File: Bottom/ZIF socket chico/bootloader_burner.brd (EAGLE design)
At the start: 65.4 x 64 mm, 6 parts, among them J1 ZIFSOCKET-28-3", Y1 16MHz

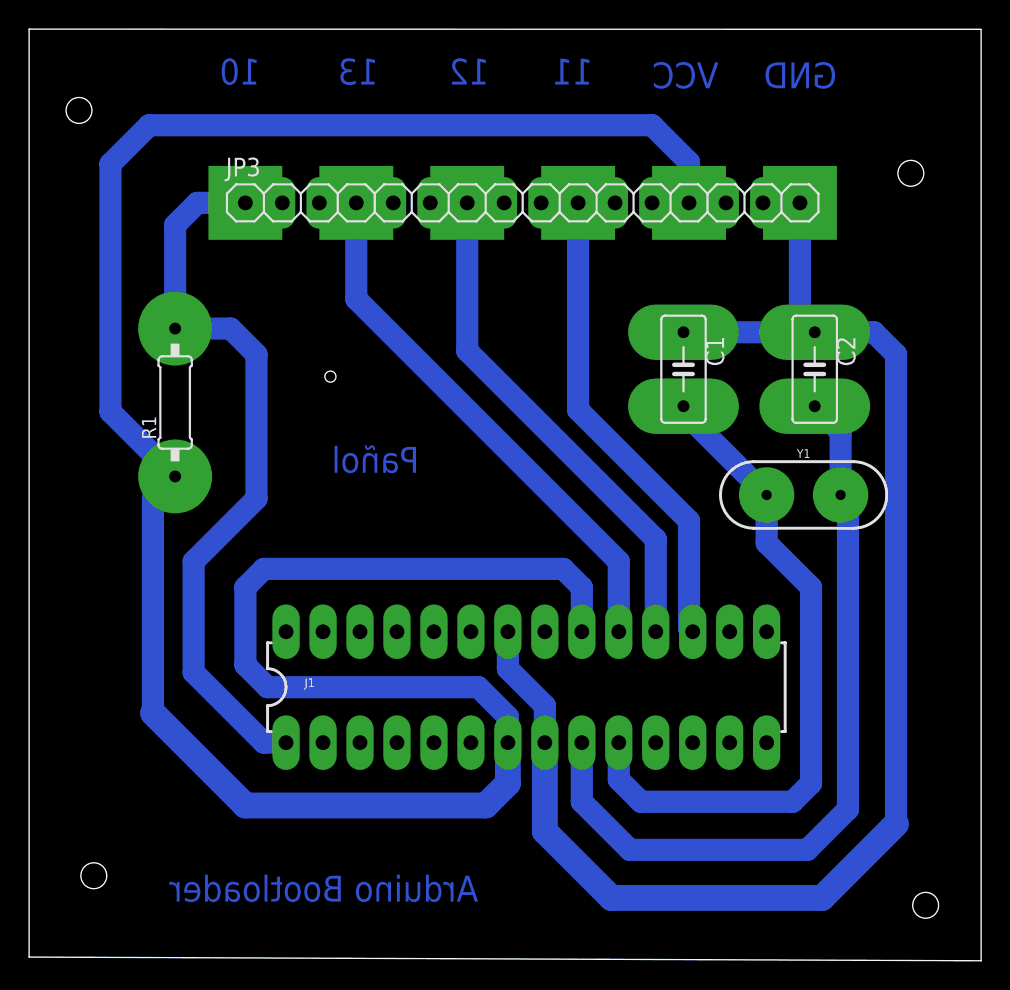
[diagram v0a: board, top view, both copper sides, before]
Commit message: Cambie la plaqueta para el zif socket chico para que queden ordenados los pines para conectar la plaqueta al Arduino
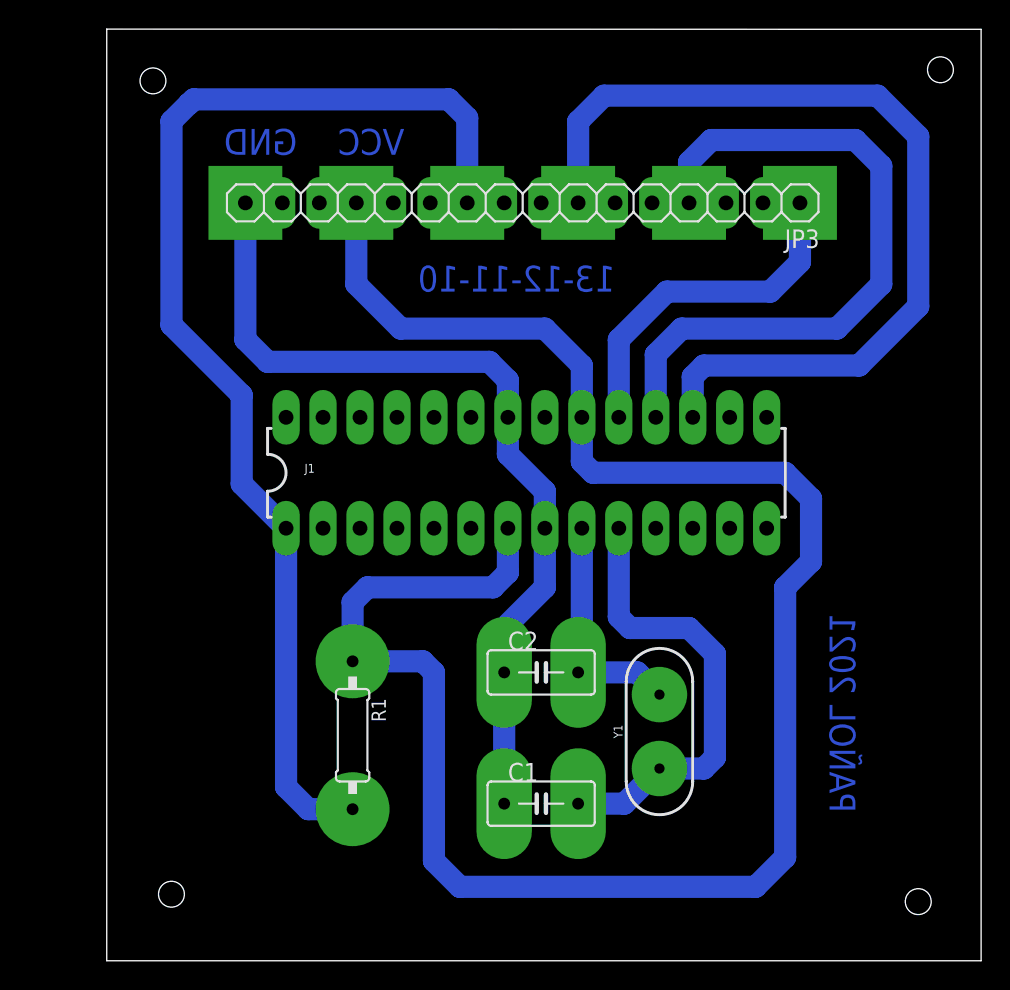
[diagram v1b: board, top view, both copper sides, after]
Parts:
- moved C1 31.4 mm to (41.1, 10.5), turned to 0 degrees
- moved C2 28.1 mm to (41.1, 19.6), turned to 0 degrees
- moved R1 25.9 mm to (28.2, 15.2), turned to 270 degrees
- moved Y1 19.0 mm to (49.3, 15.5), turned to 90 degrees
- moved J1 14.7 mm to (40.1, 33.3)
- turned JP3 to 180 degrees
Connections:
- net PIN10ARDUINO: now also JP3.10; no longer JP3.1
- net PIN11ARDUINO: now also JP3.7; no longer JP3.10
- net PIN12ARDUINO: now also JP3.4; no longer JP3.7
- net PIN13ARDUINO: now also JP3.1; no longer JP3.4
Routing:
- net GND: track 100.9 -> 59.9 mm
- net N$4: track 53.5 -> 16.2 mm
- net VCC: track 169.2 -> 135.4 mm
- net PIN10ARDUINO: track 50.9 -> 81.5 mm
- net PIN11ARDUINO: track 32.7 -> 62.8 mm
- net N$5: track 47.0 -> 31.6 mm
- net PIN13ARDUINO: track 36.9 -> 24.1 mm
- net PIN12ARDUINO: track 34.8 -> 47.7 mm
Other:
- board size 65.4 x 64 mm -> 60.1 x 64 mm
- board text added: "13-12-11-10"
- board text added: "PAÑOL 2021"
- board text removed: "10"
- board text removed: "11"
- board text removed: "12"
- board text removed: "13"
- board text removed: "Arduino Bootloader"
- board text removed: "Pañol"

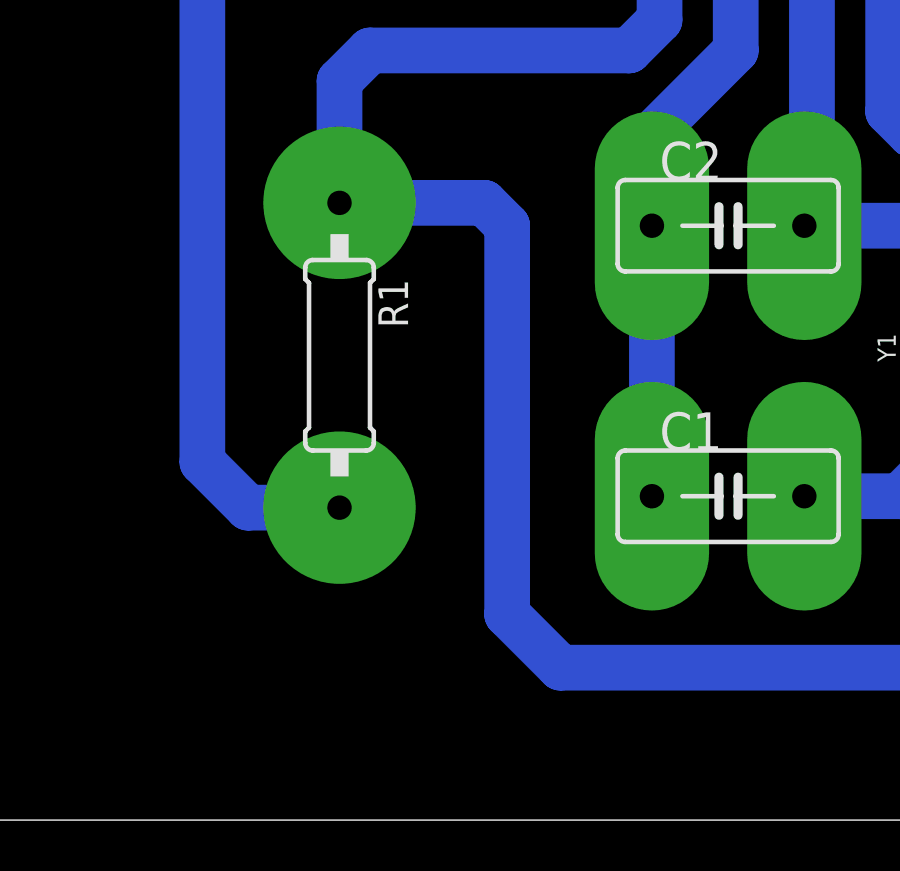
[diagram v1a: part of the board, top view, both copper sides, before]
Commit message: Cambie el diseño de la plaqueta con zif socket grande para que queden ordenados los pines con los del Arduino. Tambien cambie el dieño de la plaqueta doble (que igual hay que cambiarla poque la gracia de esa es que quede montada en el Arduino)
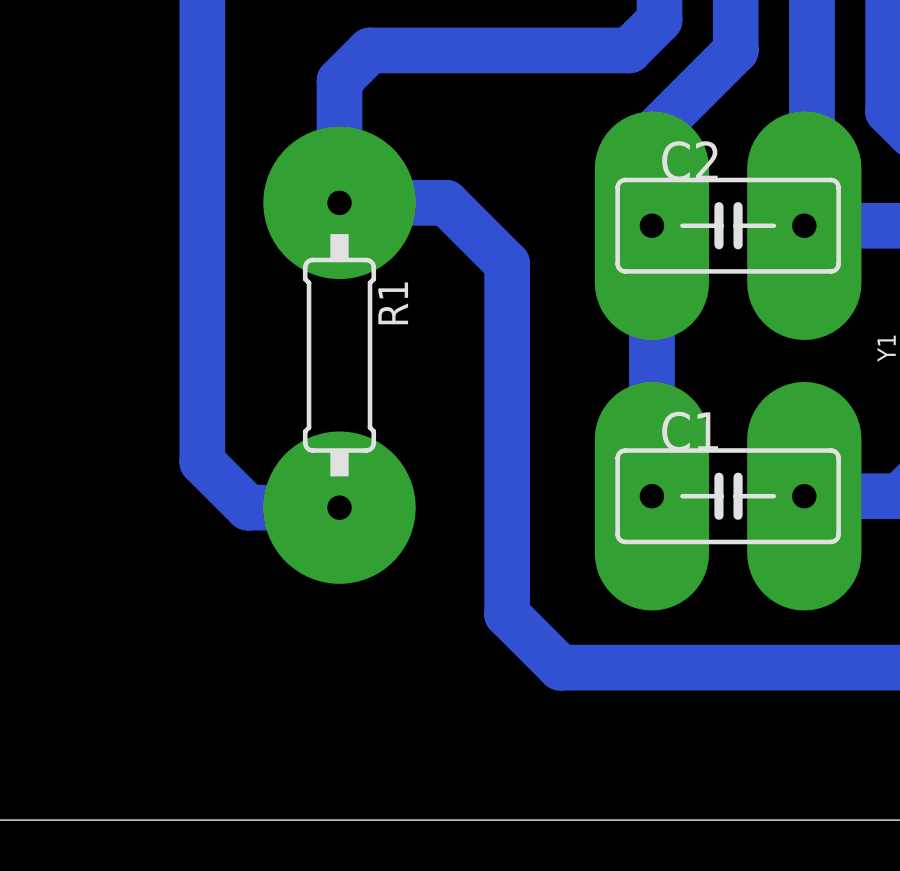
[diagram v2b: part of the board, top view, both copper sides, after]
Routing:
- net VCC: track 135.4 -> 134.6 mm
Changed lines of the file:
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@@
 <wire x1="41.402" y1="43.18" x2="31.496" y2="43.18" width="1.524" layer="16"/>
 <wire x1="31.496" y1="43.18" x2="28.448" y2="46.228" width="1.524" layer="16"/>
-<wire x1="28.194" y1="20.32" x2="33.02" y2="20.32" width="1.524" layer="16"/>
-<wire x1="33.02" y1="20.32" x2="33.782" y2="19.558" width="1.524" layer="16"/>
+<wire x1="28.194" y1="20.32" x2="31.75" y2="20.32" width="1.524" layer="16"/>
+<wire x1="31.75" y1="20.32" x2="33.782" y2="18.288" width="1.524" layer="16"/>
 <wire x1="59.69" y1="27.178" x2="59.69" y2="31.496" width="1.524" layer="16"/>
 <wire x1="59.69" y1="31.496" x2="57.912" y2="33.274" width="1.524" layer="16"/>
 <wire x1="44.704" y1="33.274" x2="43.942" y2="34.036" width="1.524" layer="16"/>
 <wire x1="43.942" y1="34.036" x2="43.942" y2="37.084" width="1.524" layer="16"/>
-<wire x1="33.782" y1="19.558" x2="33.782" y2="6.604" width="1.524" layer="16"/>
-<wire x1="33.782" y1="6.604" x2="35.56" y2="4.826" width="1.524" layer="16"/>
+<wire x1="33.782" y1="6.604" x2="33.782" y2="18.288" width="1.524" layer="16"/>
+<wire x1="35.56" y1="4.826" x2="33.782" y2="6.604" width="1.524" layer="16"/>
 <wire x1="57.912" y1="25.4" x2="59.69" y2="27.178" width="1.524" layer="16"/>
 <wire x1="57.912" y1="33.274" x2="44.704" y2="33.274" width="1.524" layer="16"/>

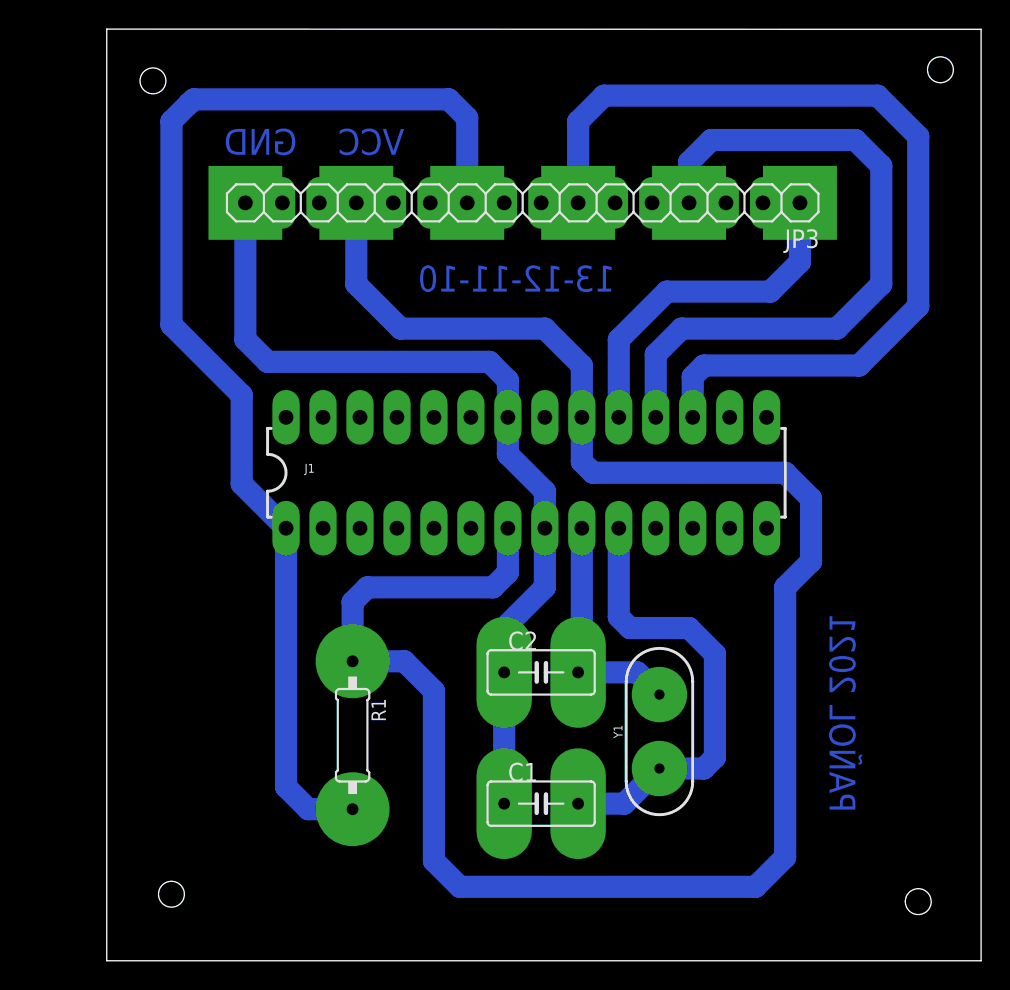
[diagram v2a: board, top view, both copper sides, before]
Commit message: Agregue las fotos nuevas de las plaquetas y agregue la lista de componentes al word
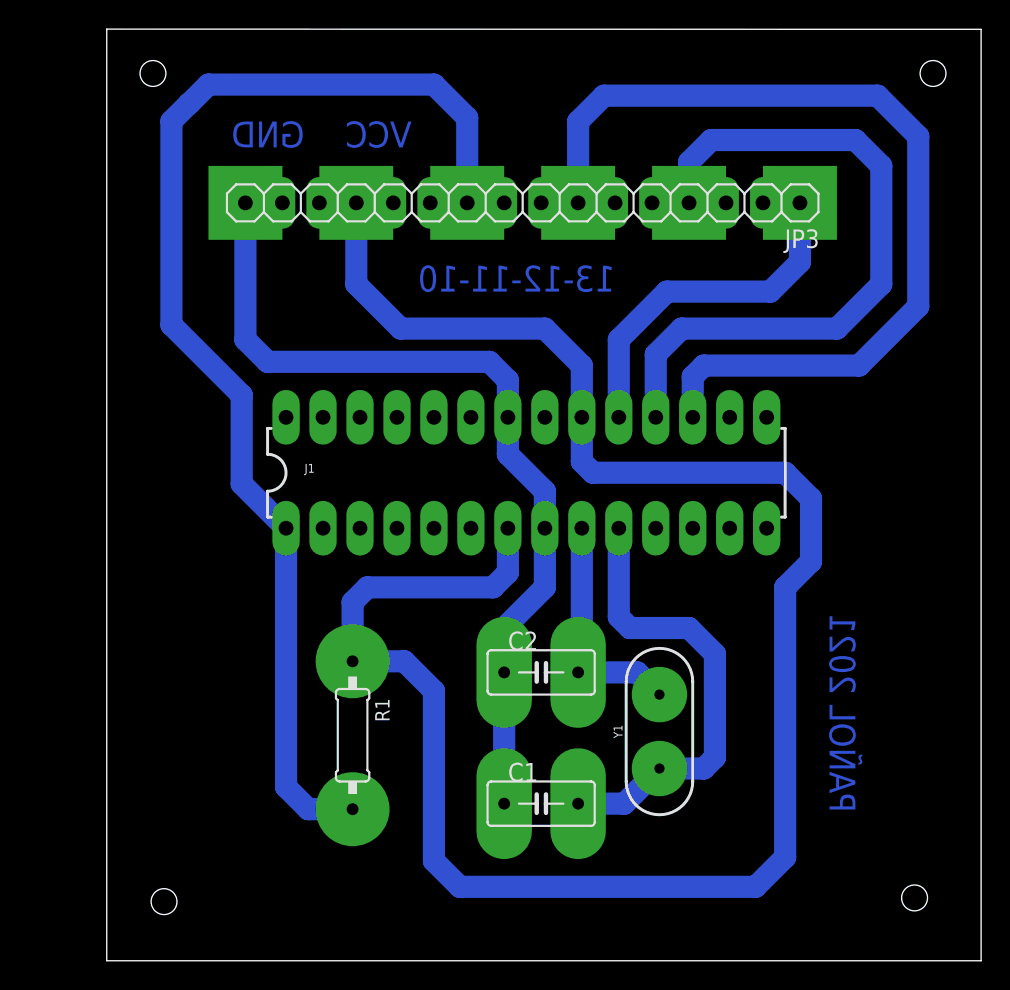
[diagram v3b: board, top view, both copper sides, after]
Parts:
- R1: value (none) -> 10K
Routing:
- net PIN10ARDUINO: track 81.5 -> 82.4 mm
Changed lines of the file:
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@@
 <wire x1="71.374" y1="-0.254" x2="71.374" y2="63.7388875" width="0" layer="20"/>
 <wire x1="71.374" y1="63.7388875" x2="11.303" y2="63.754" width="0" layer="20"/>
-<hole x="14.478" y="60.198" drill="1.778"/>
-<hole x="67.056" y="3.81" drill="1.778"/>
-<hole x="15.748" y="4.318" drill="1.778"/>
-<hole x="68.58" y="60.96" drill="1.778"/>
-<text x="31.75" y="55.118" size="1.778" layer="16" rot="MR0">VCC</text>
-<text x="24.384" y="55.118" size="1.778" layer="16" rot="MR0">GND</text>
+<hole x="14.478" y="60.706" drill="1.778"/>
+<hole x="66.802" y="4.064" drill="1.778"/>
+<hole x="15.24" y="3.81" drill="1.778"/>
+<hole x="68.072" y="60.706" drill="1.778"/>
+<text x="32.258" y="55.626" size="1.778" layer="16" rot="MR0">VCC</text>
+<text x="24.892" y="55.626" size="1.778" layer="16" rot="MR0">GND</text>
 <text x="46.228" y="45.72" size="1.778" layer="16" rot="MR0">13-12-11-10</text>
 <text x="62.738" y="23.622" size="1.778" layer="16" rot="MR270">PAÑOL 2021</text>
@@
 <attribute name="VALUE" x="24.892" y="32.004" size="0.6096" layer="27" ratio="10"/>
 </element>
-<element name="R1" library="rcl" package="0207/10" package3d_urn="urn:adsk.eagle:package:23491/2" value="" x="28.194" y="15.24" smashed="yes" rot="R270">
-<attribute name="NAME" x="29.4894" y="17.78" size="0.9906" layer="25" ratio="10" rot="R270"/>
+<element name="R1" library="rcl" package="0207/10" package3d_urn="urn:adsk.eagle:package:23491/2" value="10K" x="28.194" y="15.24" smashed="yes" rot="R270">
+<attribute name="NAME" x="29.7434" y="17.78" size="0.9906" layer="25" ratio="10" rot="R270"/>
 <attribute name="POPULARITY" value="81" x="0.254" y="-7.62" size="1.778" layer="27" rot="R270" display="off"/>
 <attribute name="SPICEPREFIX" value="R" x="0.254" y="-7.62" size="1.778" layer="27" rot="R270" display="off"/>
-<attribute name="VALUE" x="27.7114" y="16.8656" size="0.9906" layer="27" ratio="10" rot="R270"/>
+<attribute name="VALUE" x="31.5214" y="17.8816" size="0.9906" layer="27" ratio="10" rot="R270"/>
 </element>
 <element name="Y1" library="SparkFun-Clocks" package="HC49US" package3d_urn="urn:adsk.eagle:package:37515/1" value="16MHz" x="49.276" y="15.494" smashed="yes" rot="R90">
@@
 <attribute name="PROD_ID" value="XTAL-08181" x="69.596" y="51.054" size="1.778" layer="27" rot="R90" display="off"/>
 <attribute name="SF_ID" value="COM-00536" x="69.596" y="51.054" size="1.778" layer="27" rot="R90" display="off"/>
-<attribute name="VALUE" x="51.816" y="15.494" size="0.6096" layer="27" font="vector" ratio="20" rot="R90" align="top-center"/>
+<attribute name="VALUE" x="49.276" y="15.24" size="0.6096" layer="27" font="vector" ratio="20" rot="R180" align="top-center"/>
 </element>
 <element name="JP3" library="pinhead" package="1X16" package3d_urn="urn:adsk.eagle:package:22432/2" value="" x="39.878" y="51.816" smashed="yes" rot="R180">
@@
 <wire x1="20.574" y1="32.512" x2="20.574" y2="38.608" width="1.524" layer="16"/>
 <wire x1="16.9697875" y1="58.64531875" x2="16.98931875" y2="58.64531875" width="1.524" layer="16"/>
-<wire x1="16.98931875" y1="58.64531875" x2="17.272" y2="58.928" width="1.524" layer="16"/>
+<wire x1="16.98931875" y1="58.64531875" x2="18.288" y2="59.944" width="1.524" layer="16"/>
 <wire x1="15.748" y1="57.42353125" x2="16.9697875" y2="58.64531875" width="1.524" layer="16"/>
 <wire x1="36.068" y1="57.658" x2="36.068" y2="51.816" width="1.524" layer="16"/>
 <wire x1="20.574" y1="38.608" x2="15.748" y2="43.434" width="1.524" layer="16"/>
 <wire x1="15.748" y1="43.434" x2="15.748" y2="57.42353125" width="1.524" layer="16"/>
-<wire x1="17.272" y1="58.928" x2="34.798" y2="58.928" width="1.524" layer="16"/>
-<wire x1="34.798" y1="58.928" x2="36.068" y2="57.658" width="1.524" layer="16"/>
+<wire x1="18.288" y1="59.944" x2="33.782" y2="59.944" width="1.524" layer="16"/>
+<wire x1="33.782" y1="59.944" x2="36.068" y2="57.658" width="1.524" layer="16"/>
 </signal>
 </signals>
